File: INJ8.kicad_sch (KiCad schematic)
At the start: 12 parts, among them U6 VNLD5160TR-E, U7 VNLD5160TR-E, U8 VNLD5160TR-E, U9 VNLD5160TR-E

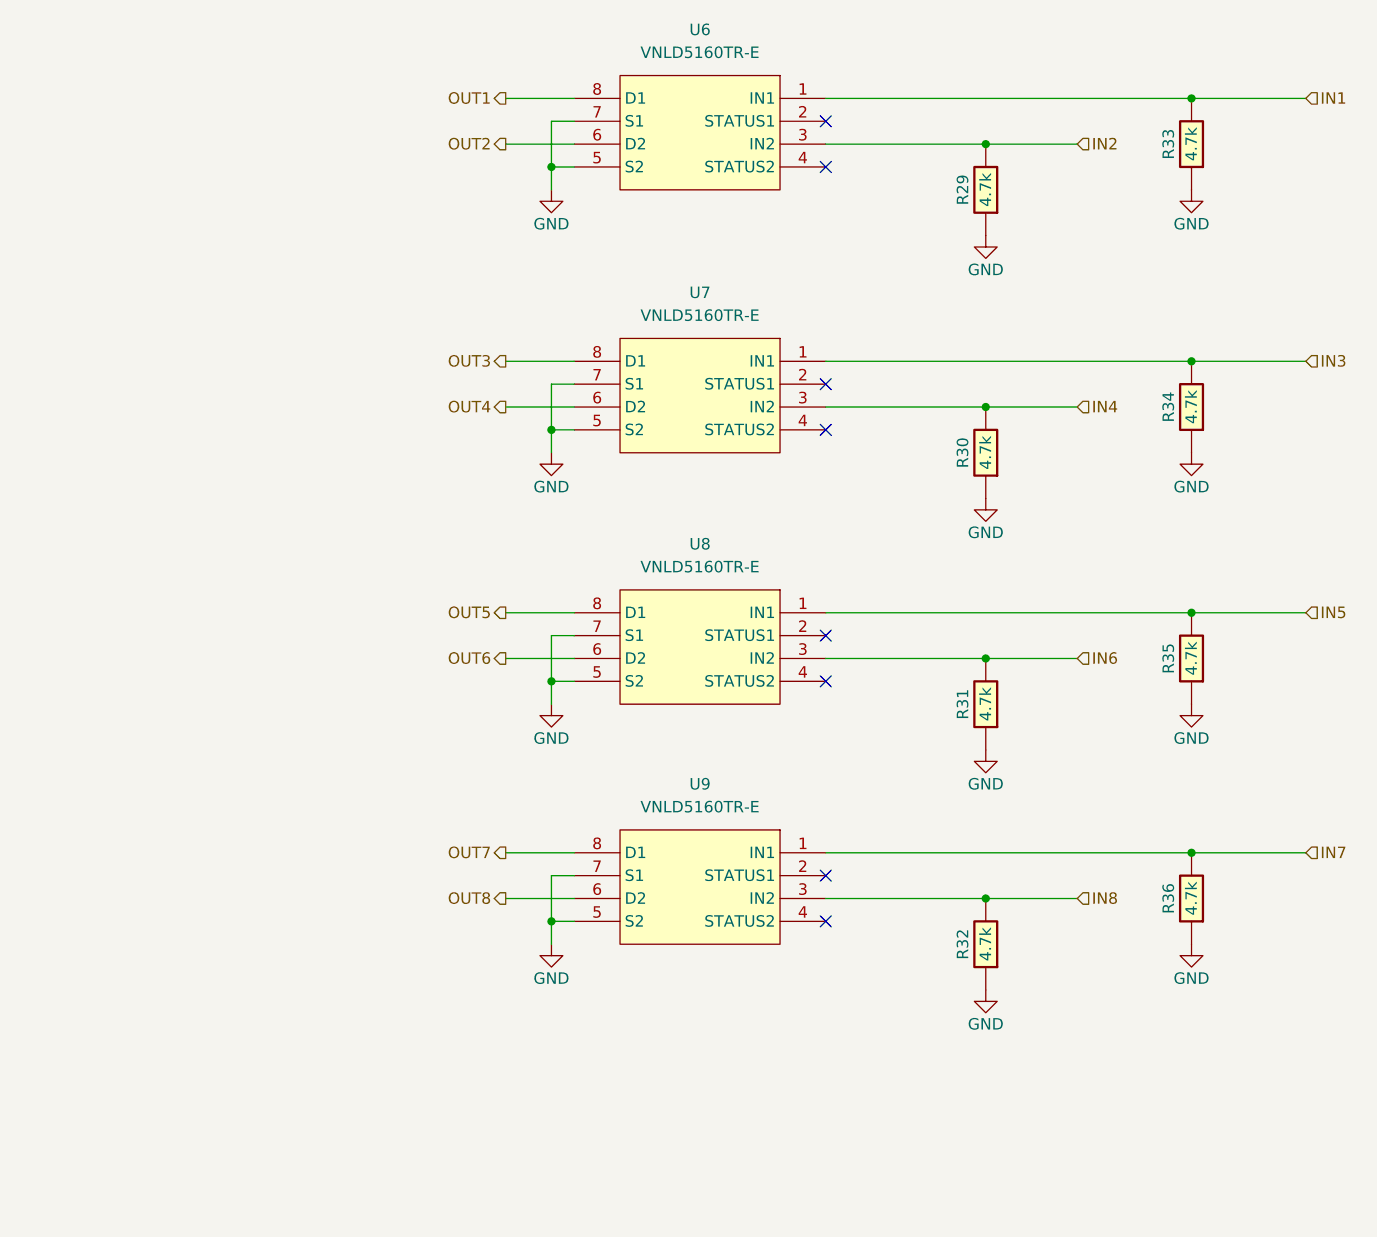
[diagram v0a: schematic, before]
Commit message: Standalone version without hellen-one
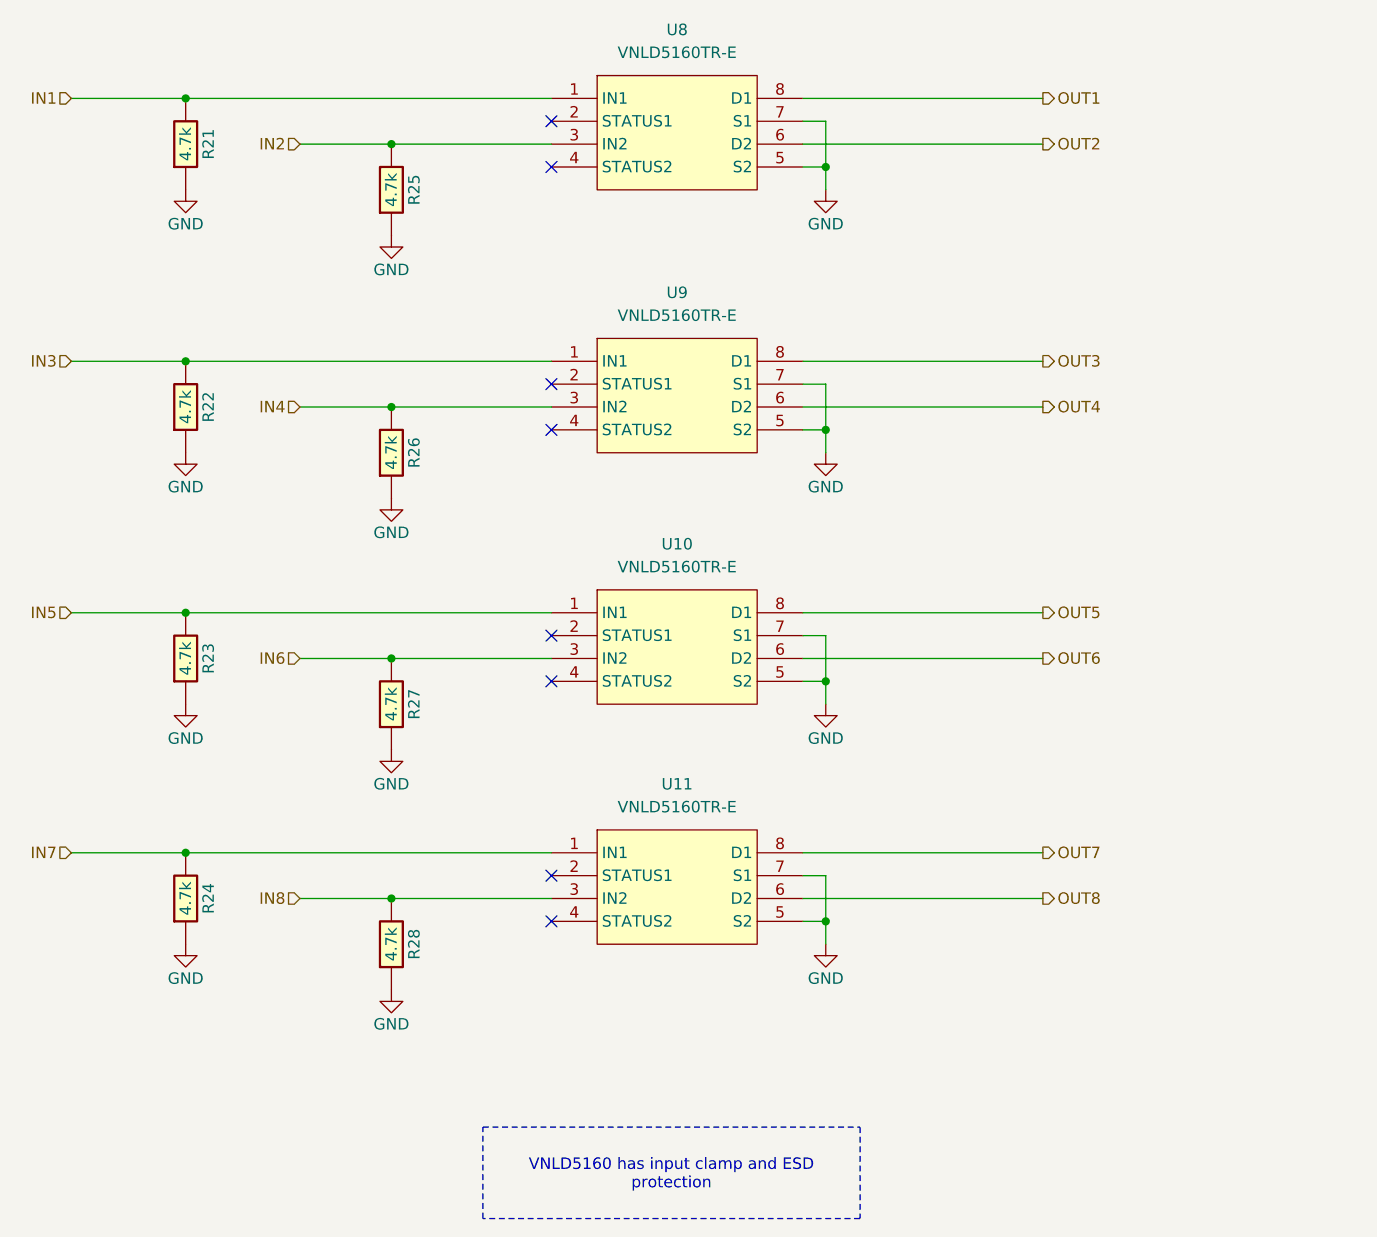
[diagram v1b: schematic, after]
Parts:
- R21: renamed from R33; footprint hellen-one-common:R0603 -> Resistor_SMD:R_0603_1608Metric
- R22: renamed from R34; footprint hellen-one-common:R0603 -> Resistor_SMD:R_0603_1608Metric
- R23: renamed from R35; footprint hellen-one-common:R0603 -> Resistor_SMD:R_0603_1608Metric
- R24: renamed from R36; footprint hellen-one-common:R0603 -> Resistor_SMD:R_0603_1608Metric
- R25: renamed from R29; footprint hellen-one-common:R0603 -> Resistor_SMD:R_0603_1608Metric
- R26: renamed from R30; footprint hellen-one-common:R0603 -> Resistor_SMD:R_0603_1608Metric
- R27: renamed from R31; footprint hellen-one-common:R0603 -> Resistor_SMD:R_0603_1608Metric
- R28: renamed from R32; footprint hellen-one-common:R0603 -> Resistor_SMD:R_0603_1608Metric
- renumbered U8 to U10, U9 to U11, U6 to U8, U7 to U9
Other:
- moved on the sheet: R21, R22, R23, R24, R25, R26, R27, R28, U10, U11, U8, U9
